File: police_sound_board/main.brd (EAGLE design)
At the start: 100 x 80 mm, 16 parts, among them U1 NE555D, U2 NE555D

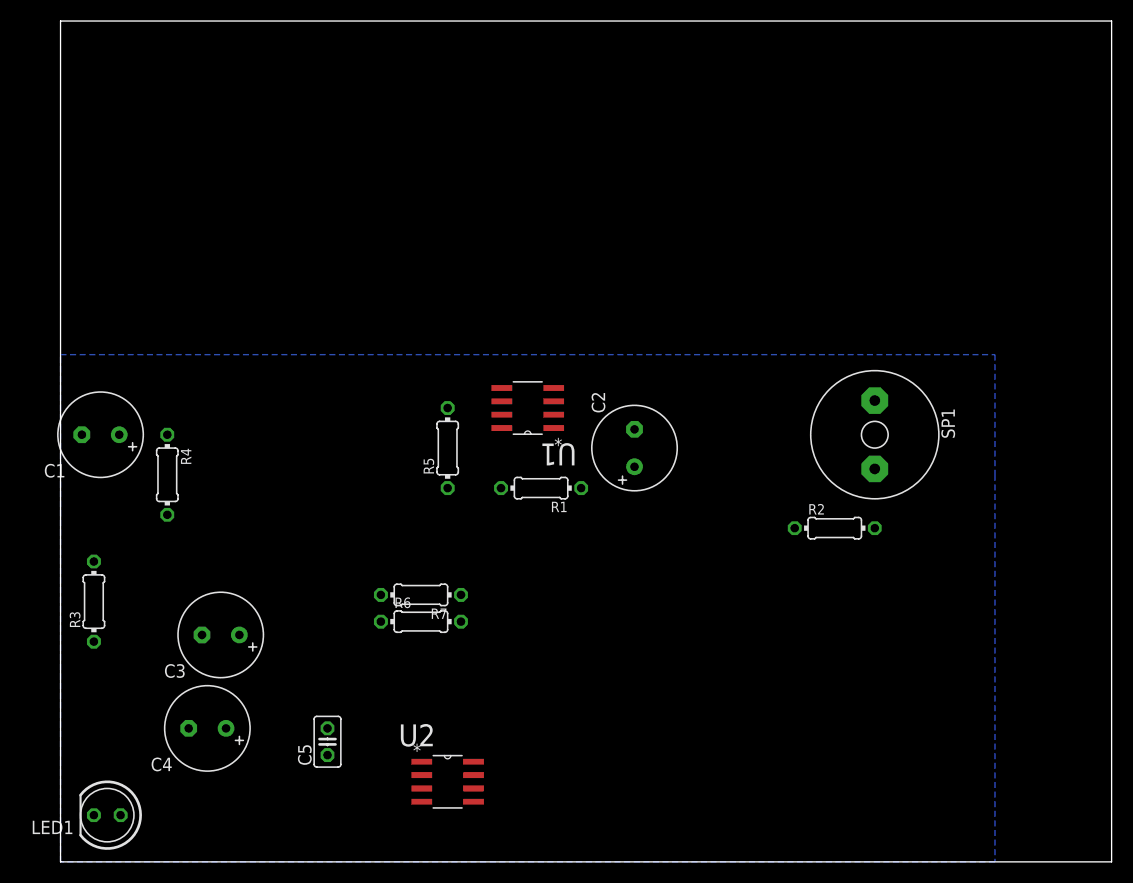
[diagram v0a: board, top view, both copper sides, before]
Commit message: removed speaker, added AOUT pin, added power connector pins
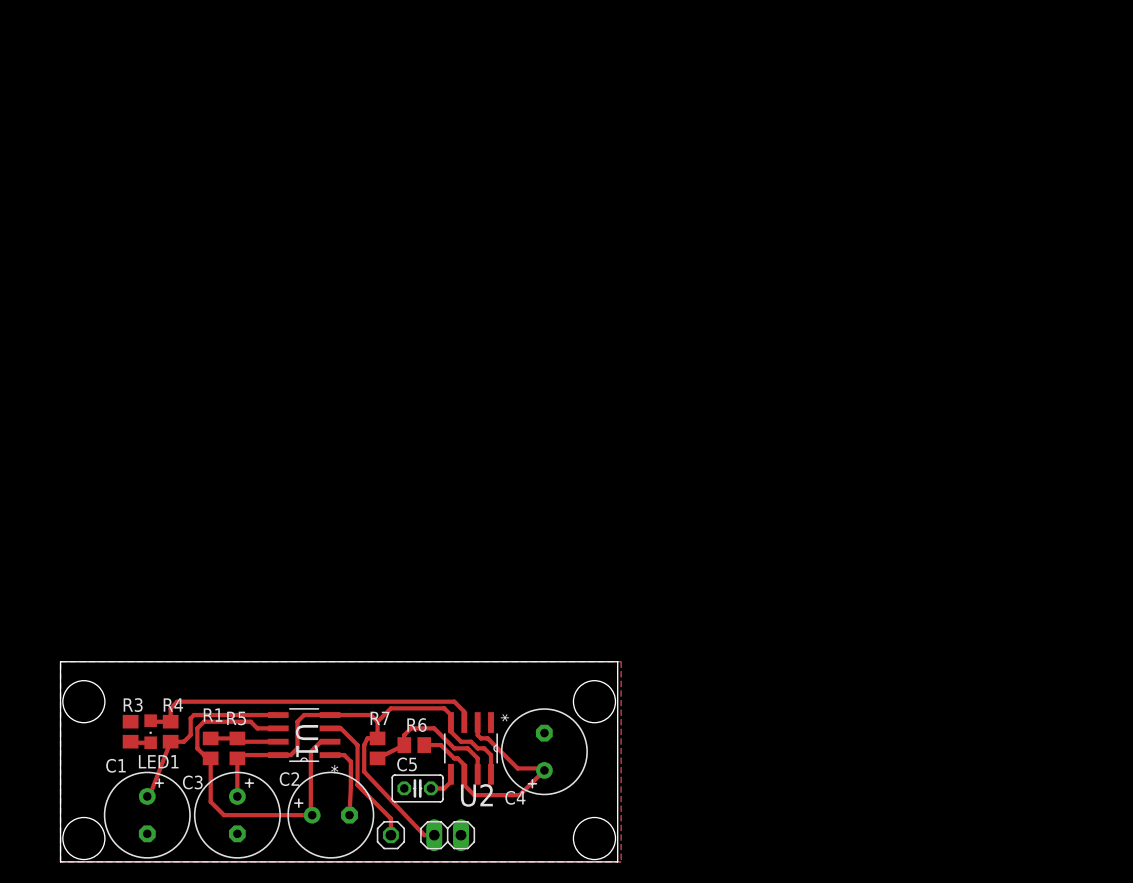
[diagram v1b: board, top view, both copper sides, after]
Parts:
- removed R2: 100, resistor:0204/7
- removed SP1: AL60P, buzzer:AL60P
- added JP1: AOUT, pinhead:1X01
- added JP2: DC, pinhead:1X02
- LED1: device led:LED5MM -> led:CHIPLED_0805
- R1, R3, R4, R5, R6, R7: device resistor:0204/7 -> resistor:R0805
- moved C2 45.3 mm to (25.7, 4.45), turned to 0 degrees
- moved R1 40.0 mm to (14.3, 10.8), turned to 90 degrees
- moved U1 37.7 mm to (23.2, 12.1)
- moved C1 36.5 mm to (8.26, 4.45), turned to 270 degrees
- moved R5 34.9 mm to (16.8, 10.8)
- moved C4 32.1 mm to (46.0, 10.5), turned to 90 degrees
- moved R4 24.4 mm to (10.5, 12.4), turned to 90 degrees
- moved C3 17.2 mm to (16.8, 4.45), turned to 270 degrees
- moved R7 15.2 mm to (30.2, 10.8), turned to 90 degrees
- moved R3 12.9 mm to (6.67, 12.4)
- moved R6 11.8 mm to (33.7, 11.1), turned to 180 degrees
- moved C5 9.66 mm to (34.0, 6.99), turned to 180 degrees
- moved LED1 8.95 mm to (8.57, 12.4)
- moved U2 3.88 mm to (39.1, 10.8), turned to 270 degrees
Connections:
- removed net N$1: R2.2, SP1.2
- net AOUT: now also JP1.1; no longer SP1.1
- net GND: now also JP2.2; no longer R2.1
- net N$7: now also LED1.C; no longer LED1.K
- net VCC: now also JP2.1
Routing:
- net VCC: track 0.00 -> 51.6 mm
- net N$4: track 0.00 -> 34.4 mm
- net TOUT: track 0.00 -> 32.8 mm
- net N$8: track 0.00 -> 24.4 mm
- net N$5: track 0.00 -> 17.9 mm
- net N$6: track 0.00 -> 13.7 mm
- net AOUT: track 0.00 -> 13.2 mm
- net GND: track 0.00 -> 7.33 mm
- net N$2: track 0.00 -> 6.74 mm
- net N$3: track 0.00 -> 2.88 mm
- net N$7: track 0.00 -> 1.95 mm
- added copper zone on layer 1, net GND
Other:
- board size 100 x 80 mm -> 53 x 19 mm
